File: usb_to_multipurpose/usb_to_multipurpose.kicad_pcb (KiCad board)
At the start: 2 copper layers, 13 parts, among them U1 FT232H

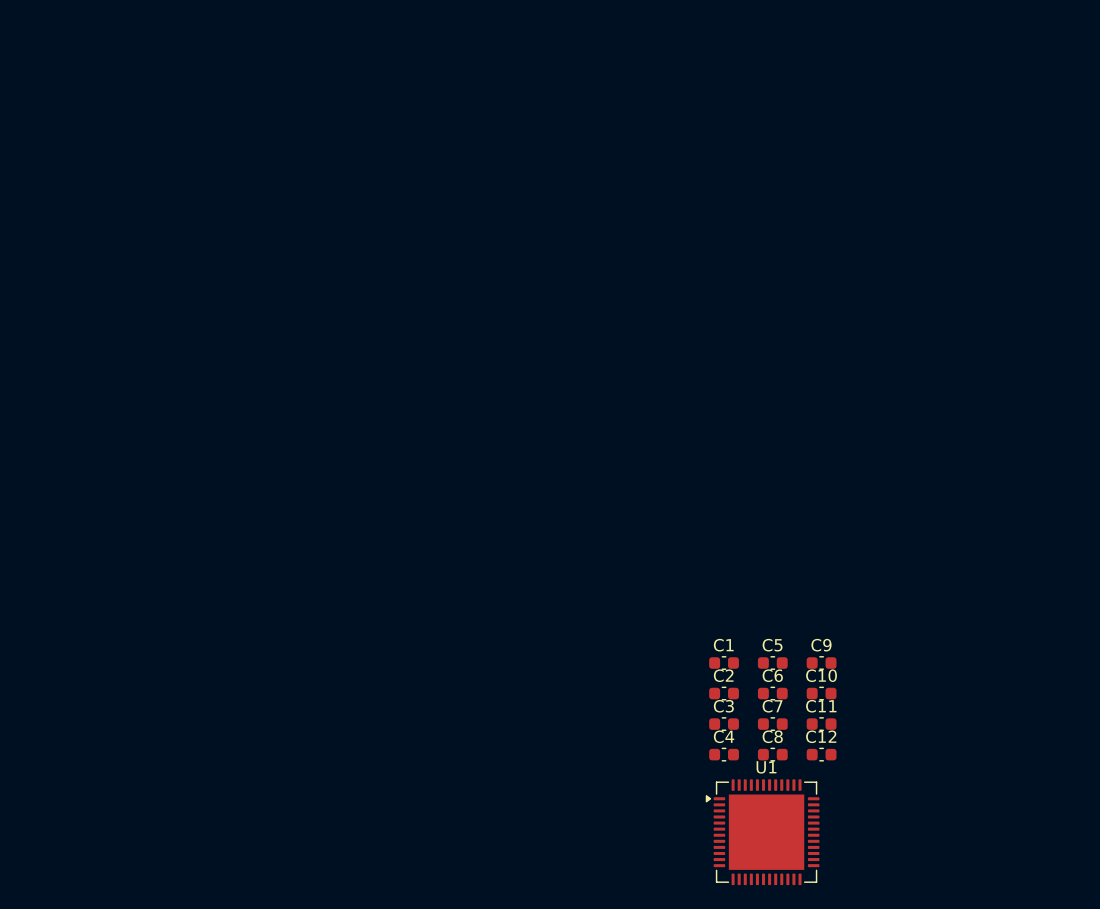
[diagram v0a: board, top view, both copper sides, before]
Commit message: Update schematic for self-powered configuration running on 3.3V. Added footprints.
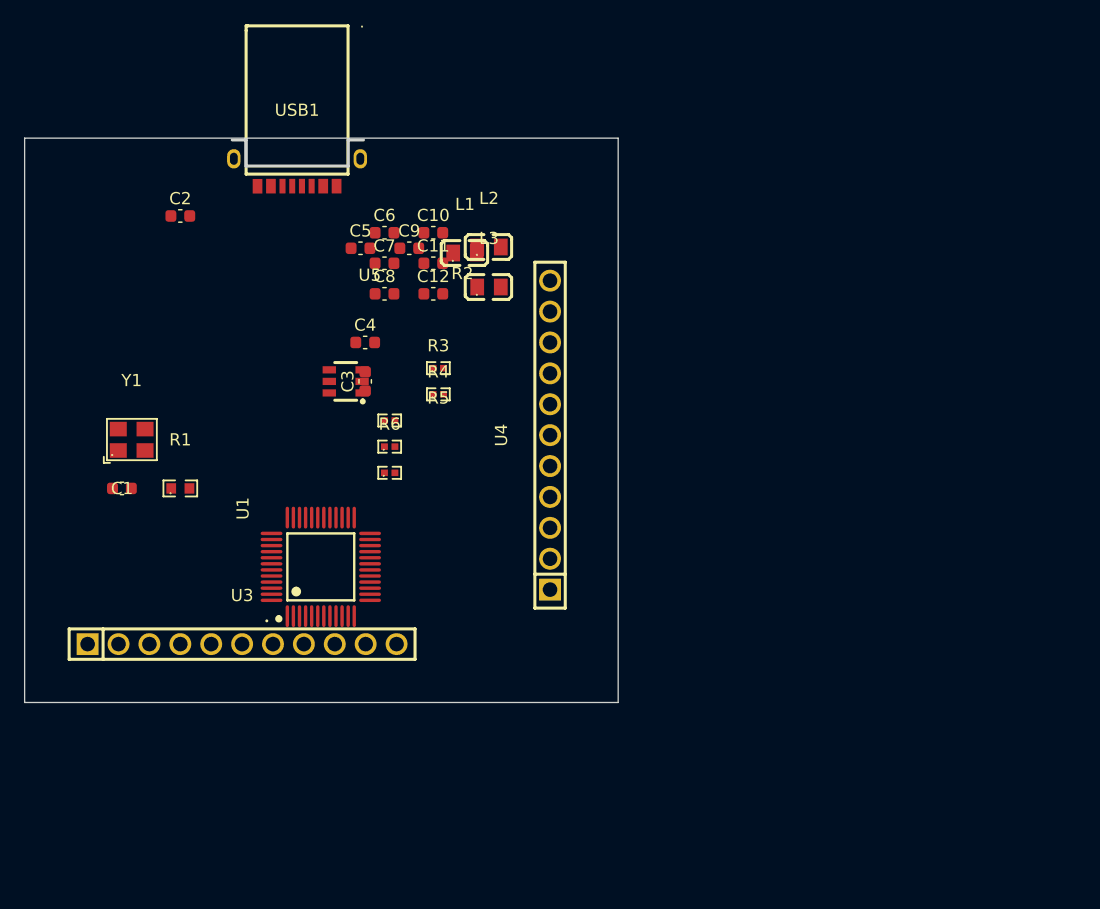
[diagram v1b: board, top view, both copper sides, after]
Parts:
- added L1: 600R/0.5A, easyeda2kicad:L0805, F.Cu at (60.2, 31.0)
- added L2: 600R/0.5A, easyeda2kicad:L0805, F.Cu at (62.2, 30.6)
- added L3: 600R/0.5A, easyeda2kicad:L0805, F.Cu at (62.2, 33.8)
- added R1: 12K 1%, easyeda2kicad:R0603, F.Cu at (36.8, 50.4)
- added R2: 2K, easyeda2kicad:R0402, F.Cu at (58.0, 40.5)
- added R3: 10K, easyeda2kicad:R0402, F.Cu at (58.0, 42.7)
- added R4: 10K, easyeda2kicad:R0402, F.Cu at (54.0, 44.8)
- added R5: 10K, easyeda2kicad:R0402, F.Cu at (54.0, 47.0)
- added R6: 10K, easyeda2kicad:R0402, F.Cu at (54.0, 49.1)
- added U3: PM2.54-1*11, easyeda2kicad:HDR-TH_11P-P2.54-V-F, F.Cu at (41.9, 63.2)
- added U4: PM2.54-1*11, easyeda2kicad:HDR-TH_11P-P2.54-V-F, F.Cu at (67.2, 46.0)
- added U5: 93LC56BT-I/OT, easyeda2kicad:SOT-23-6_L2.9-W1.6-P0.95-LS2.8-BR, F.Cu at (50.4, 41.6)
- added USB1: HYCW675-USBC12-105B, easyeda2kicad:USB-C-SMD_HYCW675-USBC12-105B, F.Cu at (46.4, 24.4)
- added Y1: 12MHz, easyeda2kicad:OSC-SMD_4P-L3.2-W2.5-BL, F.Cu at (32.8, 46.4)
- U1: footprint Package_DFN_QFN:QFN-48-1EP_8x8mm_P0.5mm_EP6.2x6.2mm -> easyeda2kicad:LQFP-48_L7.0-W7.0-P0.50-LS9.0-TL
- moved C2 59.5 mm to (36.8, 28.0)
- moved C1 51.5 mm to (32.0, 50.4), turned to 180 degrees
- moved C10 49.5 mm to (57.6, 29.4)
- moved C11 49.5 mm to (57.6, 31.9)
- moved C12 49.5 mm to (57.6, 34.4)
- moved C6 49.5 mm to (53.6, 29.4)
- moved C7 49.5 mm to (53.6, 31.9)
- moved C8 49.5 mm to (53.6, 34.4)
- moved C5 48.1 mm to (51.6, 30.7)
- moved C9 48.1 mm to (55.6, 30.7)
- moved C4 44.9 mm to (52.0, 38.4)
- moved U1 42.7 mm to (48.4, 56.9), turned to 90 degrees
- moved C3 40.8 mm to (52.0, 41.6), turned to 90 degrees
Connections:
- C5 pad 1: GND -> unconnected-(C5-Pad1)
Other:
- board outline added: 48.8 x 46.4 mm

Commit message: Add 2*8 header. Schematic cleanup.
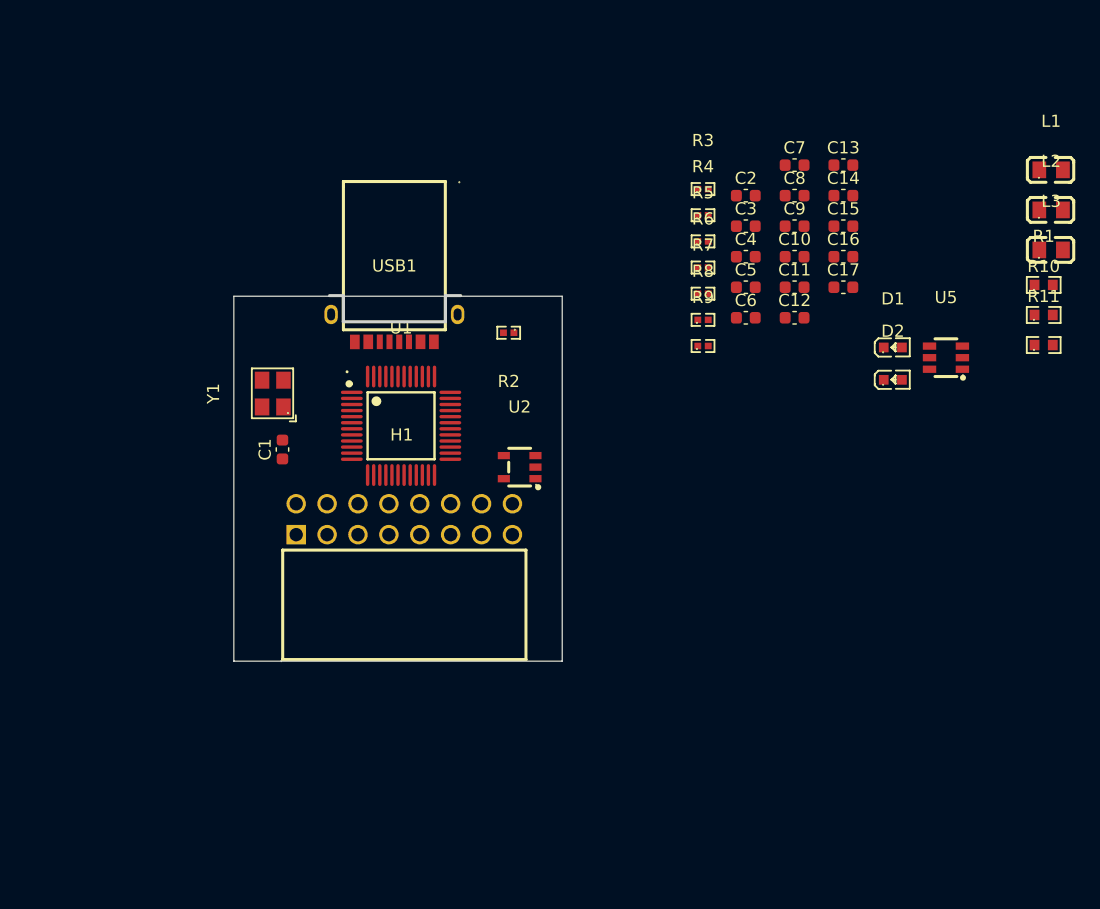
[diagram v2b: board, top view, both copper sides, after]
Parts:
- removed U3, U4: PM2.54-1*11, easyeda2kicad:HDR-TH_11P-P2.54-V-F
- added C13: 4.7uF, Capacitor_SMD:C_0603_1608Metric, F.Cu at (91.3, 23.8)
- added C14: 0.1uF, Capacitor_SMD:C_0603_1608Metric, F.Cu at (91.3, 26.3)
- added C15: 0.1uF, Capacitor_SMD:C_0603_1608Metric, F.Cu at (91.3, 28.8)
- added C16: 0.1uF, Capacitor_SMD:C_0603_1608Metric, F.Cu at (91.3, 31.4)
- added C17: 0.1uF, Capacitor_SMD:C_0603_1608Metric, F.Cu at (91.3, 33.9)
- added D1: green, easyeda2kicad:LED0603-RD, F.Cu at (95.4, 38.8)
- added D2: red, easyeda2kicad:LED0603-RD, F.Cu at (95.4, 41.5)
- added H1: HDR2.54-2*8PW, easyeda2kicad:HDR-TH_16P-P2.54-H-F-R2-C8-S2.54-W10.0, F.Cu at (55.2, 52.9)
- added R10: 12K, easyeda2kicad:R0603, F.Cu at (107.8, 36.1)
- added R11: 12K, easyeda2kicad:R0603, F.Cu at (107.8, 38.6)
- added R7: 39K, easyeda2kicad:R0402, F.Cu at (79.8, 34.4)
- added R8: 1K, easyeda2kicad:R0402, F.Cu at (79.8, 36.5)
- added R9: 1K, easyeda2kicad:R0402, F.Cu at (79.8, 38.7)
- added U2: AP2112K-3.3TRG1, easyeda2kicad:SOT-23-5_L2.9-W1.6-P0.95-LS2.7-BR, F.Cu at (64.7, 48.6)
- moved R1 72.9 mm to (107.8, 33.7)
- moved U5 49.4 mm to (99.8, 39.6)
- moved L1 48.7 mm to (108.4, 24.2)
- moved C2 46.5 mm to (83.3, 26.3)
- moved L2 46.3 mm to (108.4, 27.5)
- moved L3 46.3 mm to (108.4, 30.8)
- moved C7 34.7 mm to (87.3, 23.8)
- moved C8 34.7 mm to (87.3, 26.3)
- moved C3 33.8 mm to (83.3, 28.8), turned to 0 degrees
- moved C4 32.1 mm to (83.3, 31.4)
- moved C5 31.8 mm to (83.3, 33.9)
- moved C9 31.7 mm to (87.3, 28.8)
- moved R5 30.8 mm to (79.8, 30.1)
- moved R6 30.8 mm to (79.8, 32.2)
- moved R4 30.8 mm to (79.8, 27.9)
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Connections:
- C5 pad 1: unconnected-(C5-Pad1) -> GND
- C6 pad 2: /VREGIN -> +5V
- C7 pad 1: /VREGIN -> +5V
- L1 pad 2: /VREGIN -> +5V
- U1 pad 13: Net-(U1-ADBUS0) -> /SCL/SCK
- U1 pad 14: Net-(U1-ADBUS1) -> /SDA/MOSI
- U1 pad 15: Net-(U1-ADBUS2) -> /SDA/MISO
- U1 pad 16: Net-(U1-ADBUS3) -> /CS
- U1 pad 21: Net-(U1-ACBUS0) -> unconnected-(U1-ACBUS0-Pad21)
- U1 pad 25: Net-(U1-ACBUS1) -> unconnected-(U1-ACBUS1-Pad25)
- U1 pad 26: Net-(U1-ACBUS2) -> unconnected-(U1-ACBUS2-Pad26)
- U1 pad 27: Net-(U1-ACBUS3) -> unconnected-(U1-ACBUS3-Pad27)
- U1 pad 28: Net-(U1-ACBUS4) -> unconnected-(U1-ACBUS4-Pad28)
- U1 pad 29: Net-(U1-ACBUS5) -> unconnected-(U1-ACBUS5-Pad29)
- U1 pad 40: /VREGIN -> VCC
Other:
- board size 48.8 x 46.4 mm -> 27 x 30 mm

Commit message: Schematic refinements. Add schematic info.
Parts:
- removed C13, C7: 4.7uF, Capacitor_SMD:C_0603_1608Metric
- removed C14, C5, C6: 0.1uF, Capacitor_SMD:C_0603_1608Metric
- removed R4, R5, R6: 10K, easyeda2kicad:R0402
- moved L3 69.7 mm to (44.4, 58.4)
- moved L2 68.6 mm to (44.4, 52.2)
- moved R1 63.4 mm to (46.4, 49.4), turned to 180 degrees
- moved R10 62.7 mm to (48.8, 57.4), turned to -90 degrees
- moved R11 60.2 mm to (50.6, 57.4), turned to -90 degrees
- moved U5 55.4 mm to (44.4, 37.2)
- moved L1 53.9 mm to (57.6, 42.2)
- moved C9 48.8 mm to (43.4, 50.2), turned to 180 degrees
- moved C11 48.1 mm to (44.6, 56.0), turned to 180 degrees
- moved C10 47.2 mm to (43.4, 48.6)
- moved C12 46.3 mm to (44.6, 54.2)
- moved C2 38.4 mm to (48.0, 41.6), turned to 180 degrees
- moved D2 35.7 mm to (63.4, 57.4), turned to 90 degrees
- moved D1 34.8 mm to (66.0, 57.4), turned to 90 degrees
- moved C15 33.8 mm to (65.4, 50.6), turned to 180 degrees
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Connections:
- H1 pad 12: Net-(U1-ACBUS6) -> Net-(U1-ACBUS5)
- H1 pad 13: Net-(U1-ACBUS7) -> Net-(U1-ACBUS6)
- U1 pad 29: unconnected-(U1-ACBUS5-Pad29) -> Net-(U1-ACBUS5)
- U1 pad 40: VCC -> +5V
- USB1 pad A5: unconnected-(USB1-CC1-PadA5) -> Net-(USB1-CC1)
- USB1 pad B5: unconnected-(USB1-CC2-PadB5) -> Net-(USB1-CC2)
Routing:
- net VCC: track 0.00 -> 111.9 mm, vias 0 -> 2
- net +5V: track 0.00 -> 36.6 mm, vias 0 -> 1
- net /D+: track 0.00 -> 28.3 mm
- net Net-(D1-K): track 0.00 -> 24.3 mm, vias 0 -> 1
- net Net-(D2-K): track 0.00 -> 21.0 mm, vias 0 -> 1
- net Net-(U1-EECLK): track 0.00 -> 20.4 mm, vias 0 -> 2
- net Net-(U1-EEDATA): track 0.00 -> 20.3 mm, vias 0 -> 2
- net /D-: track 0.00 -> 17.4 mm, vias 0 -> 2
- net Net-(U1-EECS): track 0.00 -> 17.0 mm, vias 0 -> 2
- net Net-(U1-ACBUS7): track 0.00 -> 16.8 mm
- net /VPHY: track 0.00 -> 15.3 mm, vias 0 -> 2
- net Net-(U1-ADBUS6): track 0.00 -> 13.0 mm, vias 0 -> 1
- net Net-(U1-ADBUS7): track 0.00 -> 11.1 mm, vias 0 -> 1
- net Net-(U1-ACBUS6): track 0.00 -> 11.0 mm
- net Net-(U1-XCSI): track 0.00 -> 10.3 mm
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- added copper zone on B.Cu, net GND
- added copper zone on F.Cu, net GND
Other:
- board size 27 x 30 mm -> 29.8 x 32.2 mm

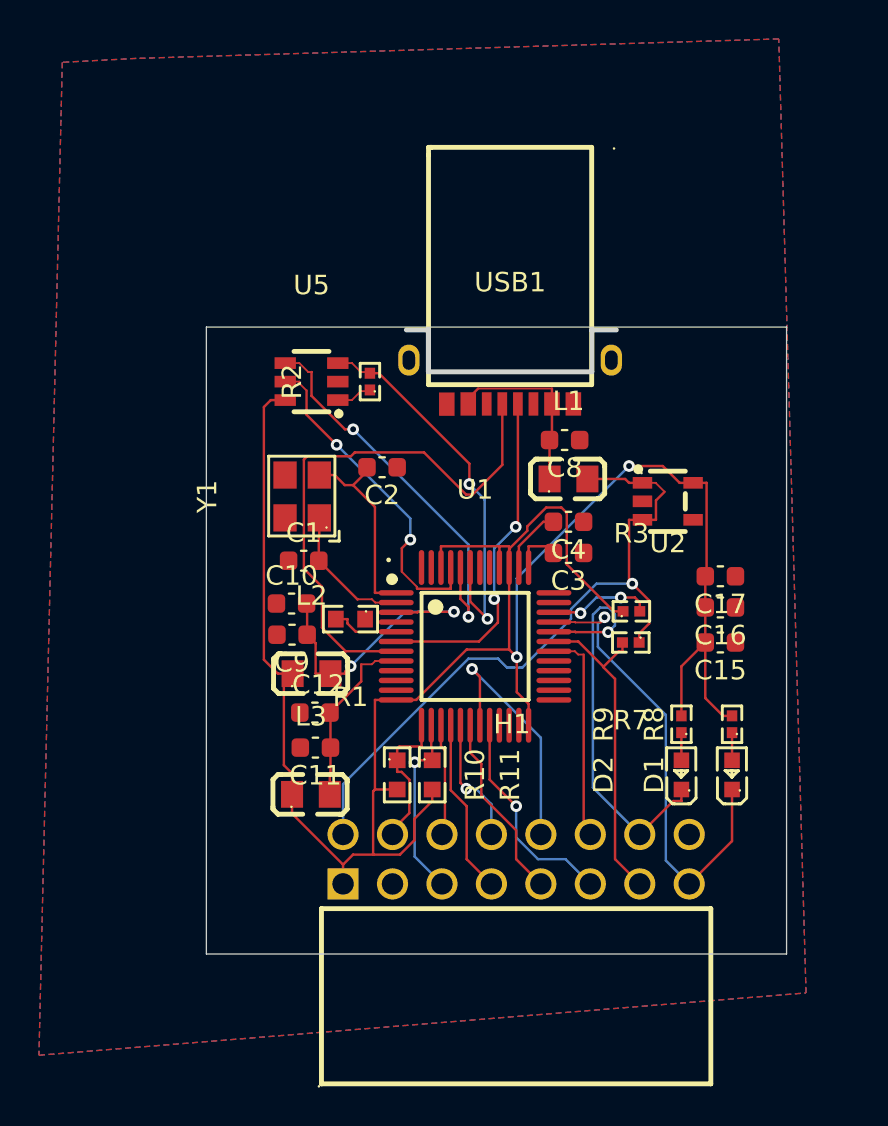
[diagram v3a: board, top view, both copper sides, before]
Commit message: Improve and define PCB shape to fit the case. Add case model.
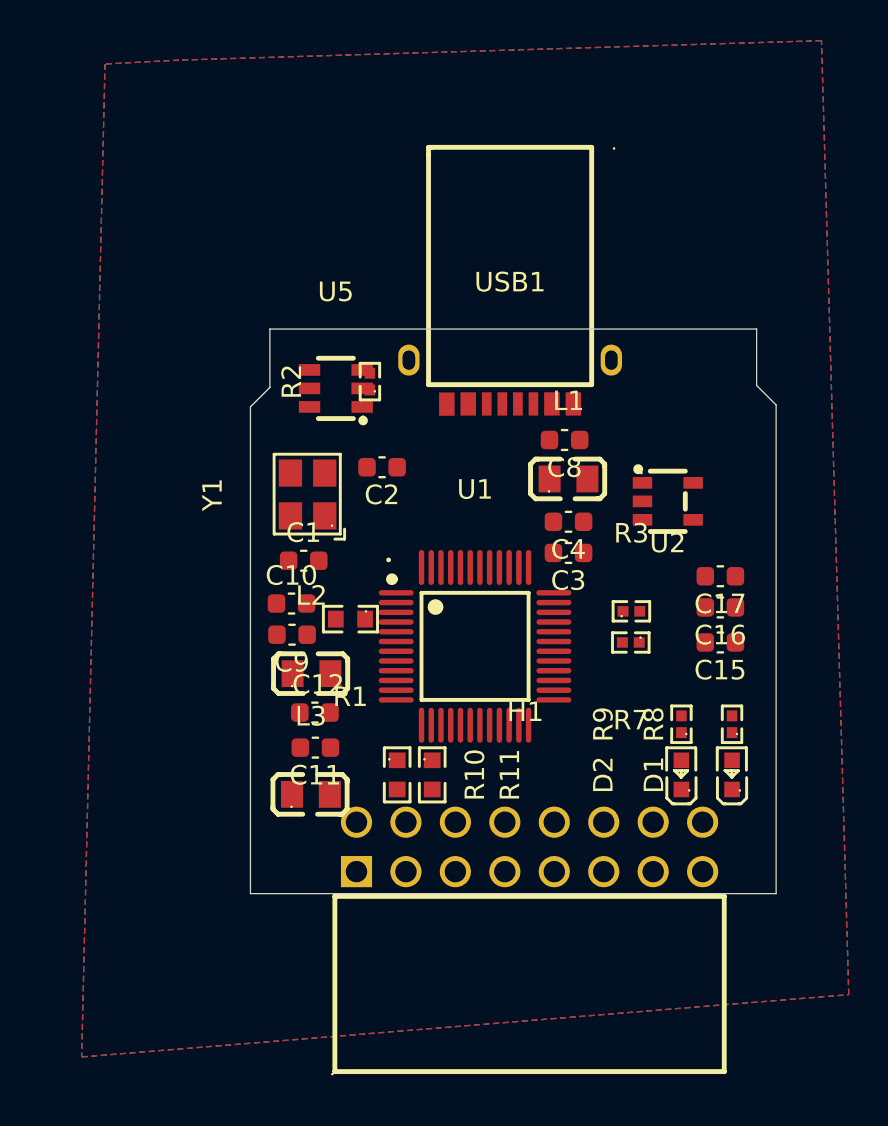
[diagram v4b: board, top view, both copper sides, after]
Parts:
- moved U5 1.30 mm to (45.6, 37.5)
- moved H1 0.93 mm to (55.6, 61.1)
- moved Y1 0.30 mm to (44.2, 43.0)
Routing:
- net VCC: track 111.9 -> 0.00 mm, vias 2 -> 0
- net +5V: track 36.6 -> 0.00 mm, vias 1 -> 0
- net /D+: track 28.3 -> 0.00 mm
- net Net-(D1-K): track 24.3 -> 0.00 mm, vias 1 -> 0
- net Net-(D2-K): track 21.0 -> 0.00 mm, vias 1 -> 0
- net Net-(U1-EECLK): track 20.4 -> 0.00 mm, vias 2 -> 0
- net Net-(U1-EEDATA): track 20.3 -> 0.00 mm, vias 2 -> 0
- net /D-: track 17.4 -> 0.00 mm, vias 2 -> 0
- net Net-(U1-EECS): track 17.0 -> 0.00 mm, vias 2 -> 0
- net Net-(U1-ACBUS7): track 16.8 -> 0.00 mm
- net /VPHY: track 15.3 -> 0.00 mm, vias 2 -> 0
- net Net-(U1-ADBUS6): track 13.0 -> 0.00 mm, vias 1 -> 0
- net Net-(U1-ADBUS7): track 11.1 -> 0.00 mm, vias 1 -> 0
- net Net-(U1-ACBUS6): track 11.0 -> 0.00 mm
- net Net-(U1-XCSI): track 10.3 -> 0.00 mm
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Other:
- board size 29.8 x 32.2 mm -> 27 x 29 mm

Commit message: Prepare v1.0 of the PCB.
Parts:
- added R4: 5K1, easyeda2kicad:R0402, F.Cu at (53.4, 40.6)
- added R5: 5K1, easyeda2kicad:R0402, F.Cu at (56.4, 40.2)
- added REF**: MountingHole_2.2mm_M2, MountingHole:MountingHole_2.2mm_M2, F.Cu at (65.0, 37.3)
- added REF**: MountingHole_2.2mm_M2, MountingHole:MountingHole_2.2mm_M2, F.Cu at (45.3, 37.3)
- C1, C11, C2, C9: footprint Capacitor_SMD:C_0603_1608Metric -> easyeda2kicad:C0402
- C10, C12, C15, C16, C17, C3, C4, C8: footprint Capacitor_SMD:C_0603_1608Metric -> easyeda2kicad:C0201
- moved R2 13.4 mm to (57.9, 45.5), turned to 0 degrees
- moved U5 11.7 mm to (55.7, 43.5)
- moved C15 9.95 mm to (63.7, 40.8), turned to -90 degrees
- moved L1 9.12 mm to (66.5, 44.2), turned to -90 degrees
- moved C16 8.54 mm to (62.5, 40.8), turned to -90 degrees
- moved C1 8.01 mm to (52.0, 46.7), turned to 90 degrees
- moved C10 7.63 mm to (51.0, 48.7)
- moved C17 7.55 mm to (61.4, 40.8), turned to -90 degrees
- moved C12 7.35 mm to (51.7, 52.4)
- moved R3 5.86 mm to (66.6, 50.0), turned to 180 degrees
- moved R7 5.77 mm to (66.5, 51.5)
- moved C4 5.59 mm to (62.5, 47.1)
- moved Y1 5.59 mm to (49.3, 45.3)
- moved U1 5.38 mm to (58.1, 51.7)
- moved C3 5.33 mm to (62.5, 48.1)
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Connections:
- H1 pad 10: Net-(U1-ADBUS6) -> Net-(U1-ADBUS5)
- H1 pad 9: Net-(U1-ADBUS5) -> Net-(U1-ADBUS6)
- USB1 pad 1: unconnected-(USB1-SHELL-Pad1) -> GND
- USB1 pad 2: unconnected-(USB1-SHELL-Pad2) -> GND
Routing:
- net VCC: track 0.00 -> 125.7 mm, vias 0 -> 5
- net +5V: track 0.00 -> 43.6 mm, vias 0 -> 3
- net /D+: track 0.00 -> 34.8 mm
- net /D-: track 0.00 -> 34.1 mm
- net GND: track 0.00 -> 31.1 mm, vias 0 -> 6
- net Net-(D2-K): track 0.00 -> 20.7 mm, vias 0 -> 1
- net Net-(D1-K): track 0.00 -> 19.7 mm, vias 0 -> 1
- net Net-(C8-Pad2): track 0.00 -> 18.3 mm, vias 0 -> 2
- net Net-(U1-ACBUS6): track 0.00 -> 13.4 mm
- net /SDA/MOSI: track 0.00 -> 11.5 mm
- net /VPHY: track 0.00 -> 10.9 mm
- net /VPLL: track 0.00 -> 10.7 mm
- net /SCL/SCK: track 0.00 -> 10.5 mm, vias 0 -> 1
- net Net-(U1-ACBUS5): track 0.00 -> 10.4 mm
- net /CS: track 0.00 -> 9.68 mm
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- removed copper zone on B.Cu, net GND
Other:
- board size 27 x 29 mm -> 27 x 29.1 mm
- board text added: "v1.0"
